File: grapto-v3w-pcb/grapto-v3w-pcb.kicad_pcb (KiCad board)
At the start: 2 copper layers, 145 x 73 mm, 60 parts, among them U11 USBLC6-4SC6, U4 USBLC6-4SC6

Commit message: Footprints done.
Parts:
- added C1: 22u, Fuse:Fuse_0603_1608Metric_Pad1.05x0.95mm_HandSolder, F.Cu at (177.4, -13.0)
- added C10: 22u, Fuse:Fuse_0603_1608Metric_Pad1.05x0.95mm_HandSolder, F.Cu at (177.4, -41.7)
- added C11: 22u, Fuse:Fuse_0603_1608Metric_Pad1.05x0.95mm_HandSolder, F.Cu at (191.4, -51.2)
- added C12: 22u, Fuse:Fuse_0603_1608Metric_Pad1.05x0.95mm_HandSolder, F.Cu at (182.7, -49.1)
- added C13: .47u, Capacitor_SMD:C_0603_1608Metric_Pad1.08x0.95mm_HandSolder, F.Cu at (187.1, -51.2)
- added C14: .1u, Capacitor_SMD:C_0603_1608Metric_Pad1.08x0.95mm_HandSolder, F.Cu at (177.4, -36.7)
- added C15: 22u, Fuse:Fuse_0603_1608Metric_Pad1.05x0.95mm_HandSolder, F.Cu at (95.3, -22.0)
- added C16: 22u, Fuse:Fuse_0603_1608Metric_Pad1.05x0.95mm_HandSolder, F.Cu at (112.0, -43.7)
- added C17: 22u, Fuse:Fuse_0603_1608Metric_Pad1.05x0.95mm_HandSolder, F.Cu at (97.5, -24.6)
- added C18: 22u, Fuse:Fuse_0603_1608Metric_Pad1.05x0.95mm_HandSolder, F.Cu at (90.9, -21.7)
- added C2: 22u, Fuse:Fuse_0603_1608Metric_Pad1.05x0.95mm_HandSolder, F.Cu at (191.4, -22.6)
- added C3: 22u, Fuse:Fuse_0603_1608Metric_Pad1.05x0.95mm_HandSolder, F.Cu at (182.7, -20.4)
- added C4: .47u, Capacitor_SMD:C_0603_1608Metric_Pad1.08x0.95mm_HandSolder, F.Cu at (187.1, -22.6)
- added C5: .1u, Capacitor_SMD:C_0603_1608Metric_Pad1.08x0.95mm_HandSolder, F.Cu at (177.4, -8.01)
- added C6: 22u, Fuse:Fuse_0603_1608Metric_Pad1.05x0.95mm_HandSolder, F.Cu at (95.3, 15.9)
- added C7: 22u, Fuse:Fuse_0603_1608Metric_Pad1.05x0.95mm_HandSolder, F.Cu at (112.0, -5.76)
- added C8: 22u, Fuse:Fuse_0603_1608Metric_Pad1.05x0.95mm_HandSolder, F.Cu at (97.5, 13.4)
- added C9: 22u, Fuse:Fuse_0603_1608Metric_Pad1.05x0.95mm_HandSolder, F.Cu at (90.9, 16.3)
- added D1: ~, Diode_SMD:D_SOD-123, F.Cu at (143.6, -14.6)
- added D10: ~, Diode_SMD:D_SOD-123, F.Cu at (155.1, -4.54)
- added D11: ~, Diode_SMD:D_SOD-123, F.Cu at (149.4, -14.6)
- added D12: ~, Diode_SMD:D_SOD-123, F.Cu at (143.6, -21.3)
- added D13: ~, Diode_SMD:D_SOD-123, F.Cu at (155.1, -7.89)
- added D14: ~, Diode_SMD:D_SOD-123, F.Cu at (155.1, -21.3)
- added D15: ~, Diode_SMD:D_SOD-123, F.Cu at (155.1, -17.9)
- added D16: ~, Diode_SMD:D_SOD-123, F.Cu at (149.4, -11.2)
- added D17: ~, Diode_SMD:D_SOD-123, F.Cu at (160.9, -11.2)
- added D18: ~, Diode_SMD:D_SOD-123, F.Cu at (155.1, -11.2)
- added D19: ~, Diode_SMD:D_SOD-123, F.Cu at (149.4, -4.54)
- added D2: ~, Diode_SMD:D_SOD-123, F.Cu at (166.6, -24.6)
- added D20: ~, Diode_SMD:D_SOD-123, F.Cu at (160.9, -14.6)
- added D21: ~, Diode_SMD:D_SOD-123, F.Cu at (155.1, -24.6)
- added D22: ~, Diode_SMD:D_SOD-123, F.Cu at (143.6, -4.54)
- added D23: ~, Diode_SMD:D_SOD-123, F.Cu at (155.1, -14.6)
- added D24: ~, Diode_SMD:D_SOD-123, F.Cu at (143.6, -7.89)
- added D25: ~, Diode_SMD:D_SOD-123, F.Cu at (143.6, -17.9)
- added D26: ~, Diode_SMD:D_SOD-123, F.Cu at (160.9, -21.3)
- added D27: ~, Diode_SMD:D_SOD-123, F.Cu at (166.6, -17.9)
- added D28: ~, Diode_SMD:D_SOD-123, F.Cu at (149.4, -24.6)
- added D29: ~, Diode_SMD:D_SOD-123, F.Cu at (160.9, -24.6)
- added D3: ~, Diode_SMD:D_SOD-123, F.Cu at (149.4, -7.89)
- added D30: LED, LED_SMD:LED_0805_2012Metric_Pad1.15x1.40mm_HandSolder, F.Cu at (177.7, -15.8)
- added D31: LED, LED_SMD:LED_0805_2012Metric_Pad1.15x1.40mm_HandSolder, F.Cu at (177.7, -44.5)
- added D32: ~, Diode_SMD:D_SOD-123, F.Cu at (143.6, -43.3)
- added D33: ~, Diode_SMD:D_SOD-123, F.Cu at (166.6, -53.3)
- added D34: ~, Diode_SMD:D_SOD-123, F.Cu at (149.4, -36.6)
- added D35: ~, Diode_SMD:D_SOD-123, F.Cu at (160.9, -46.6)
- added D36: ~, Diode_SMD:D_SOD-123, F.Cu at (149.4, -46.6)
- added D37: ~, Diode_SMD:D_SOD-123, F.Cu at (166.6, -50.0)
- added D38: ~, Diode_SMD:D_SOD-123, F.Cu at (143.6, -39.9)
- added D39: ~, Diode_SMD:D_SOD-123, F.Cu at (143.6, -53.3)
- added D4: ~, Diode_SMD:D_SOD-123, F.Cu at (160.9, -17.9)
- added D40: ~, Diode_SMD:D_SOD-123, F.Cu at (149.4, -50.0)
- added D41: ~, Diode_SMD:D_SOD-123, F.Cu at (155.1, -33.2)
- added D42: ~, Diode_SMD:D_SOD-123, F.Cu at (149.4, -43.3)
- added D43: ~, Diode_SMD:D_SOD-123, F.Cu at (143.6, -50.0)
- added D44: ~, Diode_SMD:D_SOD-123, F.Cu at (155.1, -36.6)
- added D45: ~, Diode_SMD:D_SOD-123, F.Cu at (155.1, -50.0)
- added D46: ~, Diode_SMD:D_SOD-123, F.Cu at (155.1, -46.6)
- added D47: ~, Diode_SMD:D_SOD-123, F.Cu at (149.4, -39.9)
- added D48: ~, Diode_SMD:D_SOD-123, F.Cu at (160.9, -39.9)
- added D49: ~, Diode_SMD:D_SOD-123, F.Cu at (155.1, -39.9)
- added D5: ~, Diode_SMD:D_SOD-123, F.Cu at (149.4, -17.9)
- added D50: ~, Diode_SMD:D_SOD-123, F.Cu at (149.4, -33.2)
- added D51: ~, Diode_SMD:D_SOD-123, F.Cu at (160.9, -43.3)
- added D52: ~, Diode_SMD:D_SOD-123, F.Cu at (155.1, -53.3)
- added D53: ~, Diode_SMD:D_SOD-123, F.Cu at (143.6, -33.2)
- added D54: ~, Diode_SMD:D_SOD-123, F.Cu at (155.1, -43.3)
- added D55: ~, Diode_SMD:D_SOD-123, F.Cu at (143.6, -36.6)
- added D56: ~, Diode_SMD:D_SOD-123, F.Cu at (143.6, -46.6)
- added D57: ~, Diode_SMD:D_SOD-123, F.Cu at (160.9, -50.0)
- added D58: ~, Diode_SMD:D_SOD-123, F.Cu at (166.6, -46.6)
- added D59: ~, Diode_SMD:D_SOD-123, F.Cu at (149.4, -53.3)
- added D6: ~, Diode_SMD:D_SOD-123, F.Cu at (166.6, -21.3)
- added D60: ~, Diode_SMD:D_SOD-123, F.Cu at (160.9, -53.3)
- added D7: ~, Diode_SMD:D_SOD-123, F.Cu at (143.6, -11.2)
- added D8: ~, Diode_SMD:D_SOD-123, F.Cu at (143.6, -24.6)
- added D9: ~, Diode_SMD:D_SOD-123, F.Cu at (149.4, -21.3)
- added F1: Polyfuse, Fuse:Fuse_0603_1608Metric_Pad1.05x0.95mm_HandSolder, F.Cu at (186.6, -16.5)
- added F2: Polyfuse, Fuse:Fuse_0603_1608Metric_Pad1.05x0.95mm_HandSolder, F.Cu at (93.2, 10.9)
- added F3: Polyfuse, Fuse:Fuse_0603_1608Metric_Pad1.05x0.95mm_HandSolder, F.Cu at (186.6, -45.2)
- added F4: Polyfuse, Fuse:Fuse_0603_1608Metric_Pad1.05x0.95mm_HandSolder, F.Cu at (93.2, -27.1)
- added J1: Conn_01x06_Female, grapto-v3w:df65-6P-1.7V, F.Cu at (125.4, -10.4)
- added J2: USB_C_Receptacle_USB2.0, grapto-v3w:USB_C_Receptacle_molex_2169900001, F.Cu at (112.1, -11.7)
- added J3: USB_C_Receptacle_USB2.0, grapto-v3w:USB_C_Receptacle_molex_2169900001, F.Cu at (107.5, 5.63)
- added J4: Conn_01x06_Male, Connector_PinHeader_2.54mm:PinHeader_1x06_P2.54mm_Vertical, F.Cu at (103.1, -14.7)
- added J5: Conn_01x06_Female, grapto-v3w:df65-6P-1.7V, F.Cu at (125.4, -48.3)
- added J6: USB_C_Receptacle_USB2.0, grapto-v3w:USB_C_Receptacle_molex_2169900001, F.Cu at (112.1, -49.6)
- added J7: USB_C_Receptacle_USB2.0, grapto-v3w:USB_C_Receptacle_molex_2169900001, F.Cu at (107.5, -32.3)
- added J8: Conn_01x06_Male, Connector_PinHeader_2.54mm:PinHeader_1x06_P2.54mm_Vertical, F.Cu at (103.1, -52.7)
- added JP1: SolderJumper_2_Bridged, Jumper:SolderJumper-2_P1.3mm_Bridged_RoundedPad1.0x1.5mm, F.Cu at (187.1, -19.5)
- added JP2: SolderJumper_2_Bridged, Jumper:SolderJumper-2_P1.3mm_Bridged_RoundedPad1.0x1.5mm, F.Cu at (112.0, -2.73)
- added JP3: SolderJumper_2_Bridged, Jumper:SolderJumper-2_P1.3mm_Bridged_RoundedPad1.0x1.5mm, F.Cu at (82.2, 15.9)
- added JP4: SolderJumper_2_Bridged, Jumper:SolderJumper-2_P1.3mm_Bridged_RoundedPad1.0x1.5mm, F.Cu at (187.1, -48.2)
- added JP5: SolderJumper_2_Bridged, Jumper:SolderJumper-2_P1.3mm_Bridged_RoundedPad1.0x1.5mm, F.Cu at (112.0, -40.6)
- added JP6: SolderJumper_2_Bridged, Jumper:SolderJumper-2_P1.3mm_Bridged_RoundedPad1.0x1.5mm, F.Cu at (82.2, -22.0)
- added L1: 2.2, grapto-v3w:Bourns-SRP0415, F.Cu at (87.7, 12.7)
- added L2: 2.2, grapto-v3w:Bourns-SRP0415, F.Cu at (87.7, -25.2)
- added R1: 470, Resistor_SMD:R_0603_1608Metric_Pad0.98x0.95mm_HandSolder, F.Cu at (186.3, -25.1)
- added R10: 22, Resistor_SMD:R_0603_1608Metric_Pad0.98x0.95mm_HandSolder, F.Cu at (93.2, 13.4)
- added R11: 22, Resistor_SMD:R_0603_1608Metric_Pad0.98x0.95mm_HandSolder, F.Cu at (116.3, -5.76)
- added R12: 4.7K, Resistor_SMD:R_0603_1608Metric_Pad0.98x0.95mm_HandSolder, F.Cu at (97.5, 10.9)
- added R13: 4.7K, Resistor_SMD:R_0603_1608Metric_Pad0.98x0.95mm_HandSolder, F.Cu at (116.3, -3.25)
- added R14: 470, Resistor_SMD:R_0603_1608Metric_Pad0.98x0.95mm_HandSolder, F.Cu at (86.6, 16.3)
- added R15: 470, Resistor_SMD:R_0603_1608Metric_Pad0.98x0.95mm_HandSolder, F.Cu at (186.3, -53.7)
- added R16: 2.7k, Resistor_SMD:R_0603_1608Metric_Pad0.98x0.95mm_HandSolder, F.Cu at (182.2, -44.7)
- added R17: 4.7k, Resistor_SMD:R_0603_1608Metric_Pad0.98x0.95mm_HandSolder, F.Cu at (190.6, -53.7)
- added R18: 150, Resistor_SMD:R_0603_1608Metric_Pad0.98x0.95mm_HandSolder, F.Cu at (181.8, -41.7)
- added R19: 10m, Resistor_SMD:R_0603_1608Metric_Pad0.98x0.95mm_HandSolder, F.Cu at (177.4, -39.2)
- added R2: 2.7k, Resistor_SMD:R_0603_1608Metric_Pad0.98x0.95mm_HandSolder, F.Cu at (182.2, -16.1)
- added R20: 5.1k, Resistor_SMD:R_0603_1608Metric_Pad0.98x0.95mm_HandSolder, F.Cu at (107.6, -43.7)
- added R21: 10k, Resistor_SMD:R_0603_1608Metric_Pad0.98x0.95mm_HandSolder, F.Cu at (77.9, -22.5)
- added R22: 10k, Resistor_SMD:R_0603_1608Metric_Pad0.98x0.95mm_HandSolder, F.Cu at (134.1, -53.7)
- added R23: 5.1k, Resistor_SMD:R_0603_1608Metric_Pad0.98x0.95mm_HandSolder, F.Cu at (107.6, -41.2)
- added R24: 22, Resistor_SMD:R_0603_1608Metric_Pad0.98x0.95mm_HandSolder, F.Cu at (93.2, -24.6)
- added R25: 22, Resistor_SMD:R_0603_1608Metric_Pad0.98x0.95mm_HandSolder, F.Cu at (116.3, -43.7)
- added R26: 4.7K, Resistor_SMD:R_0603_1608Metric_Pad0.98x0.95mm_HandSolder, F.Cu at (97.5, -27.1)
- added R27: 4.7K, Resistor_SMD:R_0603_1608Metric_Pad0.98x0.95mm_HandSolder, F.Cu at (116.3, -41.2)
- added R28: 470, Resistor_SMD:R_0603_1608Metric_Pad0.98x0.95mm_HandSolder, F.Cu at (86.6, -21.7)
- added R3: 4.7k, Resistor_SMD:R_0603_1608Metric_Pad0.98x0.95mm_HandSolder, F.Cu at (190.6, -25.1)
- added R4: 150, Resistor_SMD:R_0603_1608Metric_Pad0.98x0.95mm_HandSolder, F.Cu at (181.8, -13.0)
- added R5: 10m, Resistor_SMD:R_0603_1608Metric_Pad0.98x0.95mm_HandSolder, F.Cu at (177.4, -10.5)
- added R6: 5.1k, Resistor_SMD:R_0603_1608Metric_Pad0.98x0.95mm_HandSolder, F.Cu at (107.6, -5.76)
- added R7: 10k, Resistor_SMD:R_0603_1608Metric_Pad0.98x0.95mm_HandSolder, F.Cu at (77.9, 15.4)
- added R8: 10k, Resistor_SMD:R_0603_1608Metric_Pad0.98x0.95mm_HandSolder, F.Cu at (134.1, -15.8)
- added R9: 5.1k, Resistor_SMD:R_0603_1608Metric_Pad0.98x0.95mm_HandSolder, F.Cu at (107.6, -3.25)
- added TP1: TestPoint, TestPoint:TestPoint_Pad_2.0x2.0mm, F.Cu at (181.7, -9.75)
- added TP10: TestPoint, TestPoint:TestPoint_Pad_2.0x2.0mm, F.Cu at (181.7, -38.4)
- added TP11: TestPoint, TestPoint:TestPoint_Pad_2.0x2.0mm, F.Cu at (186.0, -41.5)
- added TP12: TestPoint, TestPoint:TestPoint_Pad_2.0x2.0mm, F.Cu at (191.2, -47.9)
- added TP13: TestPoint, TestPoint:TestPoint_Pad_2.0x2.0mm, F.Cu at (125.8, -44.5)
- added TP14: TestPoint, TestPoint:TestPoint_Pad_2.0x2.0mm, F.Cu at (101.7, -25.6)
- added TP15: TestPoint, TestPoint:TestPoint_Pad_2.0x2.0mm, F.Cu at (120.5, -39.9)
- added TP16: TestPoint, TestPoint:TestPoint_Pad_2.0x2.0mm, F.Cu at (134.0, -50.5)
- added TP17: TestPoint, TestPoint:TestPoint_Pad_2.0x2.0mm, F.Cu at (105.8, -25.6)
- added TP18: TestPoint, TestPoint:TestPoint_Pad_2.0x2.0mm, F.Cu at (109.8, -25.6)
- added TP2: TestPoint, TestPoint:TestPoint_Pad_2.0x2.0mm, F.Cu at (186.0, -12.8)
- added TP3: TestPoint, TestPoint:TestPoint_Pad_2.0x2.0mm, F.Cu at (191.2, -19.3)
- added TP4: TestPoint, TestPoint:TestPoint_Pad_2.0x2.0mm, F.Cu at (125.8, -6.53)
- added TP5: TestPoint, TestPoint:TestPoint_Pad_2.0x2.0mm, F.Cu at (101.7, 12.4)
- added TP6: TestPoint, TestPoint:TestPoint_Pad_2.0x2.0mm, F.Cu at (120.5, -1.98)
- added TP7: TestPoint, TestPoint:TestPoint_Pad_2.0x2.0mm, F.Cu at (134.0, -12.5)
- added TP8: TestPoint, TestPoint:TestPoint_Pad_2.0x2.0mm, F.Cu at (105.8, 12.4)
- added TP9: TestPoint, TestPoint:TestPoint_Pad_2.0x2.0mm, F.Cu at (109.8, 12.4)
- added U1: AP9211S-AL, grapto-v3w:U-DFN2030-6_type_c, F.Cu at (177.5, -23.8)
- added U10: MAX17260TFDN, Package_DFN_QFN:DFN-14-1EP_3x3mm_P0.4mm_EP1.78x2.35mm, F.Cu at (181.6, -52.7)
- added U12: ACN52840, grapto-v3w:ACN52840_mirror, F.Cu at (87.4, -39.2)
- added U13: TPS2110, Package_SO:TSSOP-8_4.4x3mm_P0.65mm, F.Cu at (80.1, -26.0)
- added U14: LM3676SD-3.3, Package_SON:WSON-8-1EP_3x3mm_P0.5mm_EP1.6x2.0mm, F.Cu at (121.3, -44.2)
- added U2: MCP7383x-2xMC, Package_DFN_QFN:DFN-8-1EP_3x2mm_P0.5mm_EP1.75x1.45mm, F.Cu at (177.9, -19.1)
- added U3: MAX17260TFDN, Package_DFN_QFN:DFN-14-1EP_3x3mm_P0.4mm_EP1.78x2.35mm, F.Cu at (181.6, -24.0)
- added U5: ACN52840, grapto-v3w:ACN52840_mirror, F.Cu at (87.4, -1.25)
- added U6: TPS2110, Package_SO:TSSOP-8_4.4x3mm_P0.65mm, F.Cu at (80.1, 11.9)
- added U7: LM3676SD-3.3, Package_SON:WSON-8-1EP_3x3mm_P0.5mm_EP1.6x2.0mm, F.Cu at (121.3, -6.28)
- added U8: AP9211S-AL, grapto-v3w:U-DFN2030-6_type_c, F.Cu at (177.5, -52.4)
- added U9: MCP7383x-2xMC, Package_DFN_QFN:DFN-8-1EP_3x2mm_P0.5mm_EP1.75x1.45mm, F.Cu at (177.9, -47.8)
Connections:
- SW1 pad 1: ROW0 -> /Right/row0
- SW10 pad 1: ROW1 -> /Right/row1
- SW11 pad 1: ROW1 -> /Right/row1
- SW12 pad 1: ROW2 -> /Right/row2
- SW13 pad 1: ROW2 -> /Right/row2
- SW14 pad 1: ROW2 -> /Right/row2
- SW15 pad 1: ROW2 -> /Right/row2
- SW16 pad 1: ROW2 -> /Right/row2
- SW17 pad 1: ROW2 -> /Right/row2
- SW18 pad 1: ROW3 -> /Right/row3
- SW19 pad 1: ROW3 -> /Right/row3
- SW2 pad 1: ROW0 -> /Right/row0
- SW20 pad 1: ROW3 -> /Right/row3
- SW21 pad 1: ROW3 -> /Right/row3
- SW22 pad 1: ROW3 -> /Right/row3
- SW23 pad 1: ROW3 -> /Right/row3
- SW24 pad 1: ROW4 -> /Right/row4
- SW25 pad 1: ROW4 -> /Right/row4
- SW26 pad 1: ROW4 -> /Right/row4
- SW27 pad 1: ROW4 -> /Right/row4
- SW28 pad 1: ROW4 -> /Right/row4
- SW29 pad 1: ROW4 -> /Right/row4
- SW3 pad 1: ROW0 -> /Right/row0
- SW30 pad 1: ROW0 -> /Left/row0
- SW31 pad 1: ROW0 -> /Left/row0
- SW32 pad 1: ROW0 -> /Left/row0
- SW33 pad 1: ROW0 -> /Left/row0
- SW34 pad 1: ROW0 -> /Left/row0
- SW35 pad 1: ROW1 -> /Left/row1
- SW36 pad 1: ROW1 -> /Left/row1
- SW37 pad 1: ROW1 -> /Left/row1
- SW38 pad 1: ROW1 -> /Left/row1
- SW39 pad 1: ROW1 -> /Left/row1
- SW4 pad 1: ROW0 -> /Right/row0
- SW40 pad 1: ROW1 -> /Left/row1
- SW41 pad 1: ROW2 -> /Left/row2
- SW42 pad 1: ROW2 -> /Left/row2
- SW43 pad 1: ROW2 -> /Left/row2
- SW44 pad 1: ROW2 -> /Left/row2
- SW45 pad 1: ROW2 -> /Left/row2
- SW46 pad 1: ROW2 -> /Left/row2
- SW47 pad 1: ROW3 -> /Left/row3
- SW48 pad 1: ROW3 -> /Left/row3
- SW49 pad 1: ROW3 -> /Left/row3
- SW5 pad 1: ROW0 -> /Right/row0
- SW50 pad 1: ROW3 -> /Left/row3
- SW51 pad 1: ROW3 -> /Left/row3
- SW52 pad 1: ROW3 -> /Left/row3
- SW53 pad 1: ROW4 -> /Left/row4
- SW54 pad 1: ROW4 -> /Left/row4
- SW55 pad 1: ROW4 -> /Left/row4
- SW56 pad 1: ROW4 -> /Left/row4
- SW57 pad 1: ROW4 -> /Left/row4
- SW58 pad 1: ROW4 -> /Left/row4
- SW6 pad 1: ROW1 -> /Right/row1
- SW7 pad 1: ROW1 -> /Right/row1
- SW8 pad 1: ROW1 -> /Right/row1
- SW9 pad 1: ROW1 -> /Right/row1
- U11 pad 2: SYSGND -> /Left/sysgnd
- U11 pad 5: VBUS -> /Left/vusb
- U4 pad 2: SYSGND -> /Right/sysgnd
- U4 pad 5: VBUS -> /Right/vusb

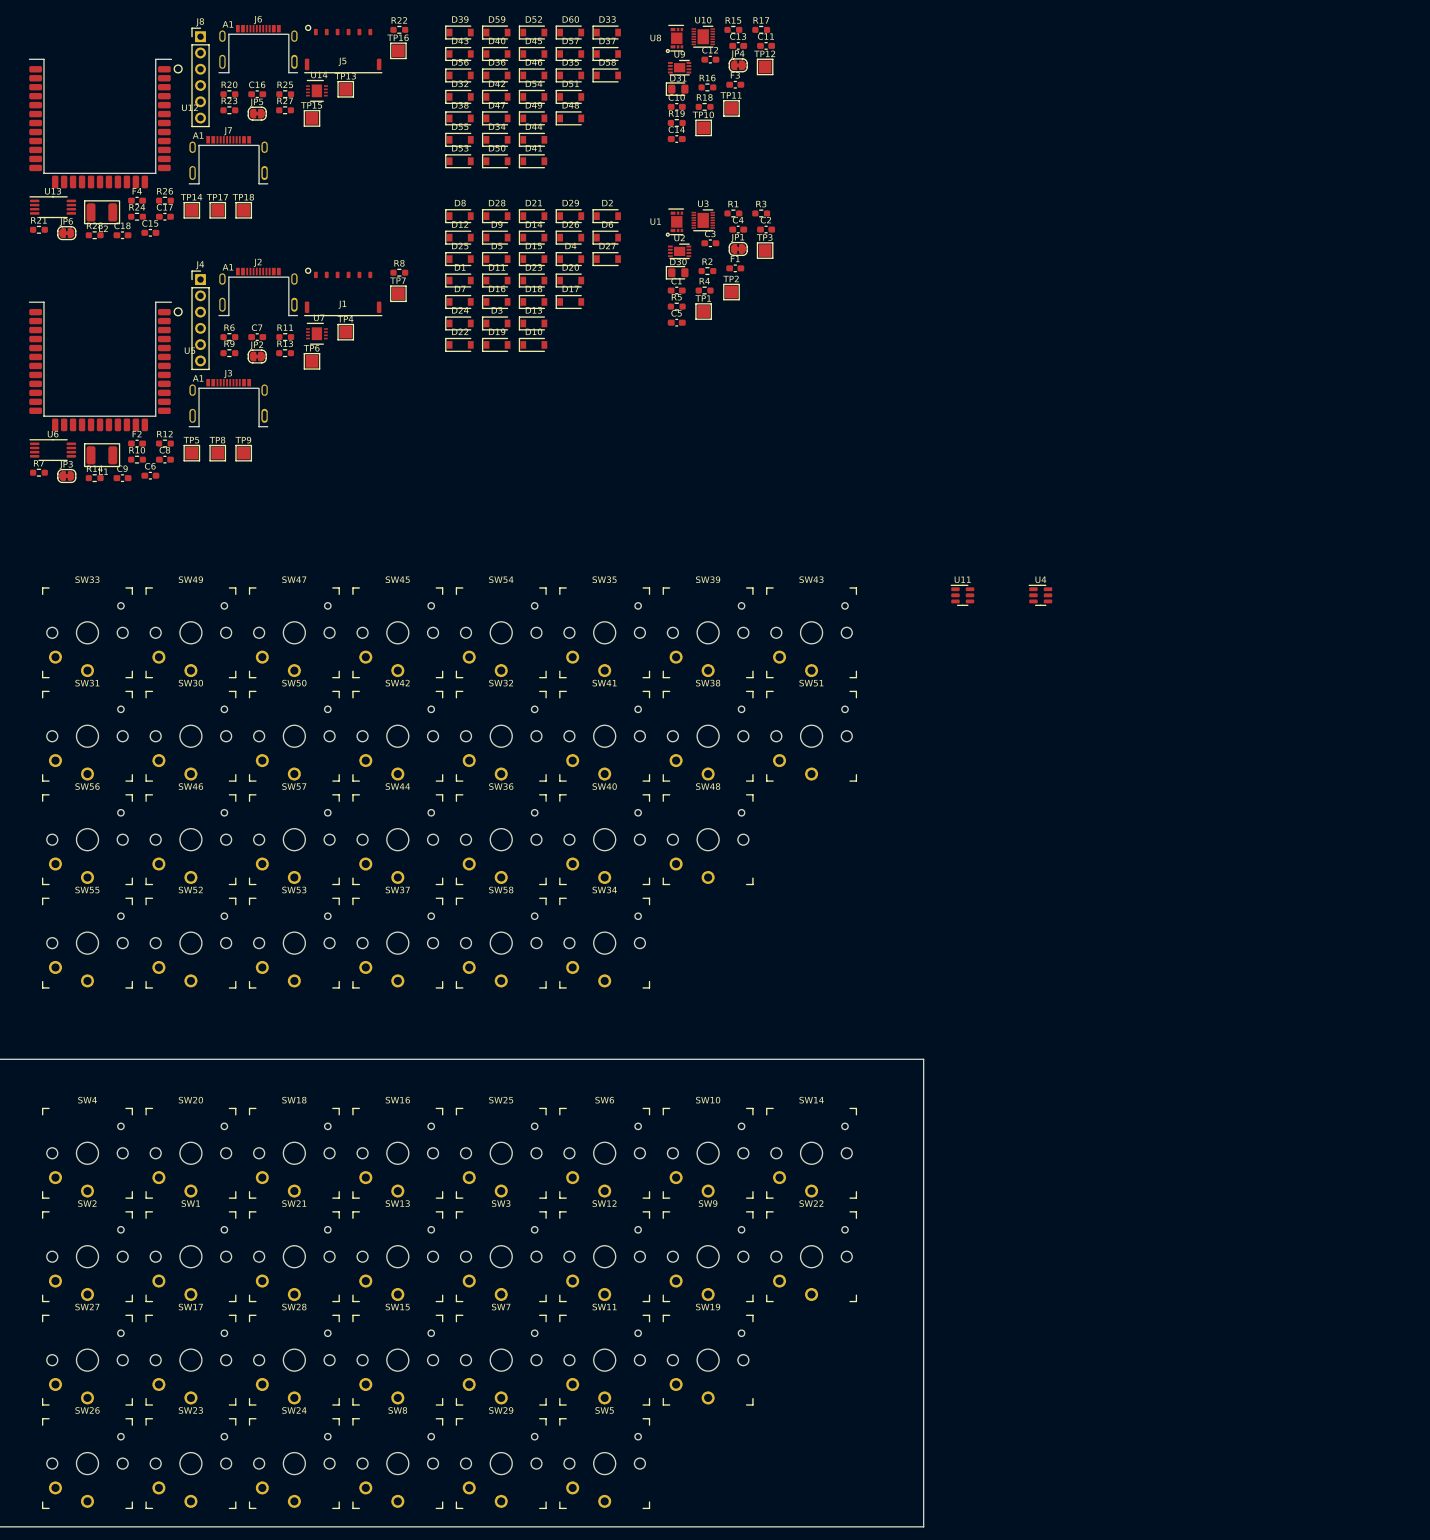
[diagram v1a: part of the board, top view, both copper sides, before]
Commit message: Fixed 3d model paths for pcb.
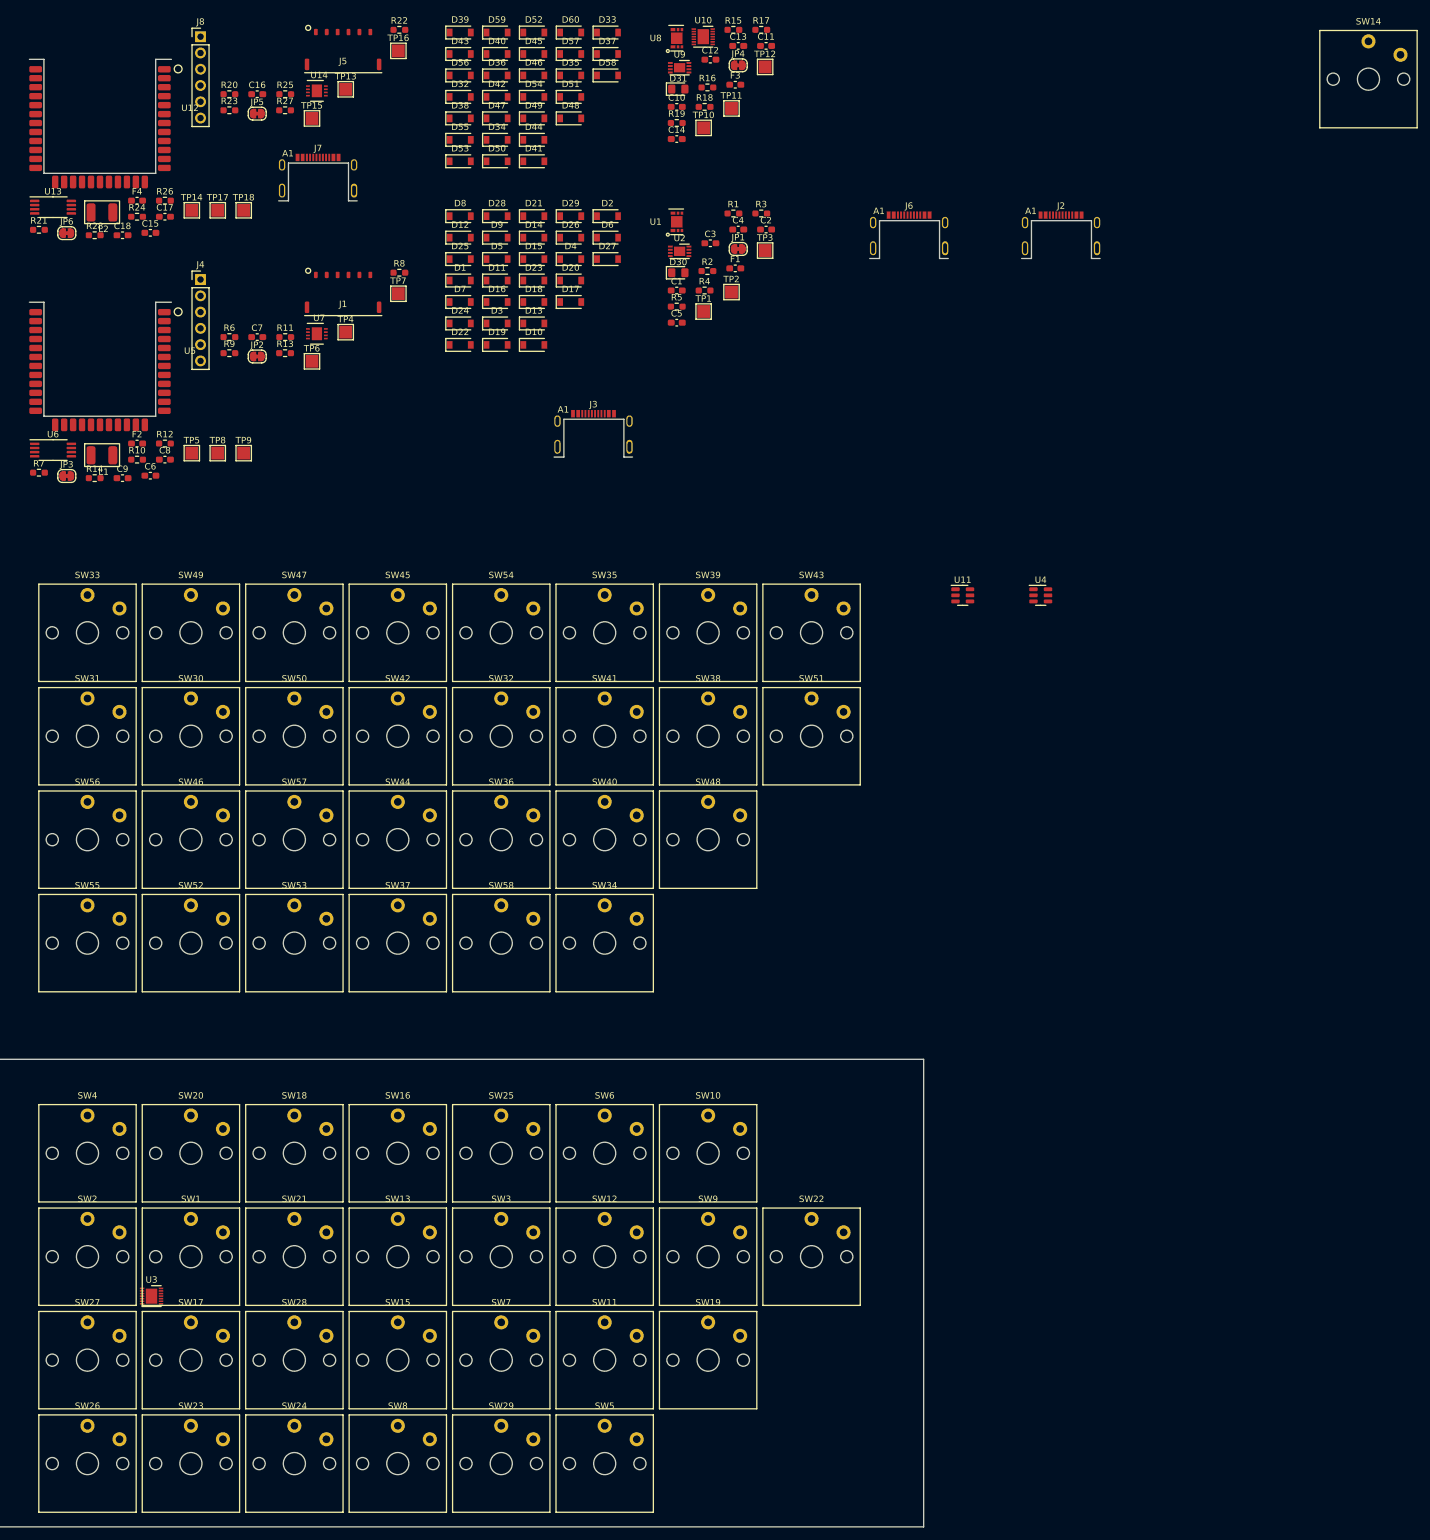
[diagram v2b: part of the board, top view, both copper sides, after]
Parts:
- SW1, SW10, SW11, SW12, SW13, SW14, SW15, SW16, SW17, SW18, SW19, SW2, SW20, SW21, SW22, SW23, SW24, SW25, SW26, SW27, SW28, SW29, SW3, SW30, SW31, SW32, SW33, SW34, SW35, SW36, SW37, SW38, SW39, SW4, SW40, SW41, SW42, SW43, SW44, SW45, SW46, SW47, SW48, SW49, SW5, SW50, SW51, SW52, SW53, SW54, SW55, SW56, SW57, SW58, SW6, SW7, SW8, SW9: footprint choc:SW_PG1350 -> Switch_Keyboard_Kailh:SW_Kailh_Choc_V1_1.00u
- moved SW14 188.9 mm to (285.4, -46.0)
- moved U3 188.8 mm to (95.5, 144.0)
- moved J2 125.5 mm to (237.4, -18.0)
- moved J6 106.4 mm to (213.7, -18.0)
- moved J3 57.4 mm to (164.4, 13.0)
- moved J7 14.9 mm to (121.5, -27.0)
